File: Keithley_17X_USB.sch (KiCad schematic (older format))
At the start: 39 parts, among them J1 USB_B, J2 SIGNAL INPUT, J3 PROG, U1 TLP281-4, U2 TLP281-4, U3 MIC5504-3.3YM5, U4 MSP430FR2110, U5 FT230XS

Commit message: add right angle mount
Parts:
- H5, H6: footprint (none) -> Terminal_Keystone:Keystone_Screw-Terminal_7761_RightAngle; Description (none) -> TERM SCREW M3 4 PIN PCB RA; Manufacture (none) -> Keystone Electronics; Mfg Part Number (none) -> 7761; Supplier (none) -> Digi-Key; Supplier Part Number (none) -> 36-7761-ND
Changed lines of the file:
@@
 F 0 "H5" H 6900 6100 50  0000 C CNN
 F 1 "M3_RA" H 6900 6025 50  0000 C CNN
-F 2 "" H 6900 5900 50  0001 C CNN
-F 3 "~" H 6900 5900 50  0001 C CNN
+F 2 "Terminal_Keystone:Keystone_Screw-Terminal_7761_RightAngle" H 6900 5900 50  0001 C CNN
+F 3 "http://www.keyelco.com/product-pdf.cfm?p=3928" H 6900 5900 50  0001 C CNN
+F 4 "TERM SCREW M3 4 PIN PCB RA" H 6900 5900 50  0001 C CNN "Description"
+F 5 "Keystone Electronics" H 6900 5900 50  0001 C CNN "Manufacture"
+F 6 "7761" H 6900 5900 50  0001 C CNN "Mfg Part Number"
+F 7 "Digi-Key" H 6900 5900 50  0001 C CNN "Supplier"
+F 8 "36-7761-ND" H 6900 5900 50  0001 C CNN "Supplier Part Number"
 	1    6900 5900
 	1    0    0    -1
@@
 $Comp
 L Mechanical:MountingHole H6
-U 1 1 5C6C11B3
+U 1 1 5C6C2A25
 P 7300 5900
 F 0 "H6" H 7300 6100 50  0000 C CNN
 F 1 "M3_RA" H 7300 6025 50  0000 C CNN
-F 2 "" H 7300 5900 50  0001 C CNN
-F 3 "~" H 7300 5900 50  0001 C CNN
+F 2 "Terminal_Keystone:Keystone_Screw-Terminal_7761_RightAngle" H 7300 5900 50  0001 C CNN
+F 3 "http://www.keyelco.com/product-pdf.cfm?p=3928" H 7300 5900 50  0001 C CNN
+F 4 "TERM SCREW M3 4 PIN PCB RA" H 7300 5900 50  0001 C CNN "Description"
+F 5 "Keystone Electronics" H 7300 5900 50  0001 C CNN "Manufacture"
+F 6 "7761" H 7300 5900 50  0001 C CNN "Mfg Part Number"
+F 7 "Digi-Key" H 7300 5900 50  0001 C CNN "Supplier"
+F 8 "36-7761-ND" H 7300 5900 50  0001 C CNN "Supplier Part Number"
 	1    7300 5900
 	1    0    0    -1

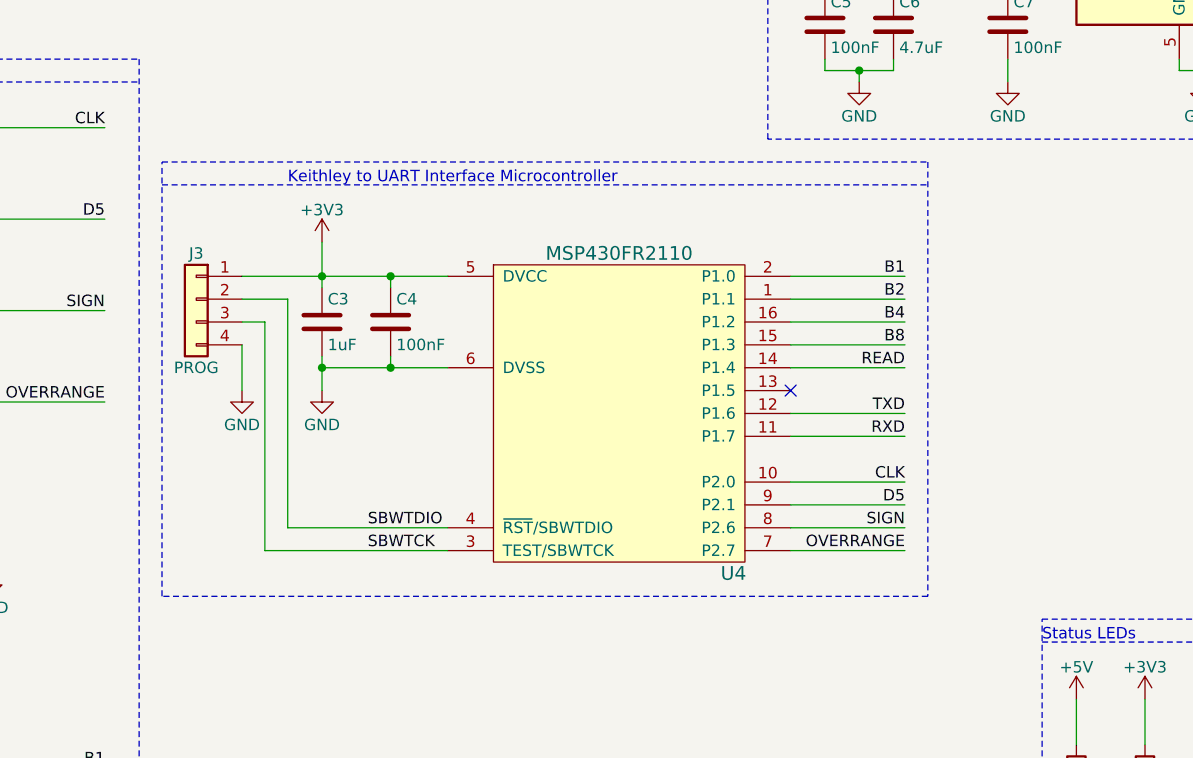
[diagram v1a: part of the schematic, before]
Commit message: added rate selection, trigger on clk or D5. Future implementation
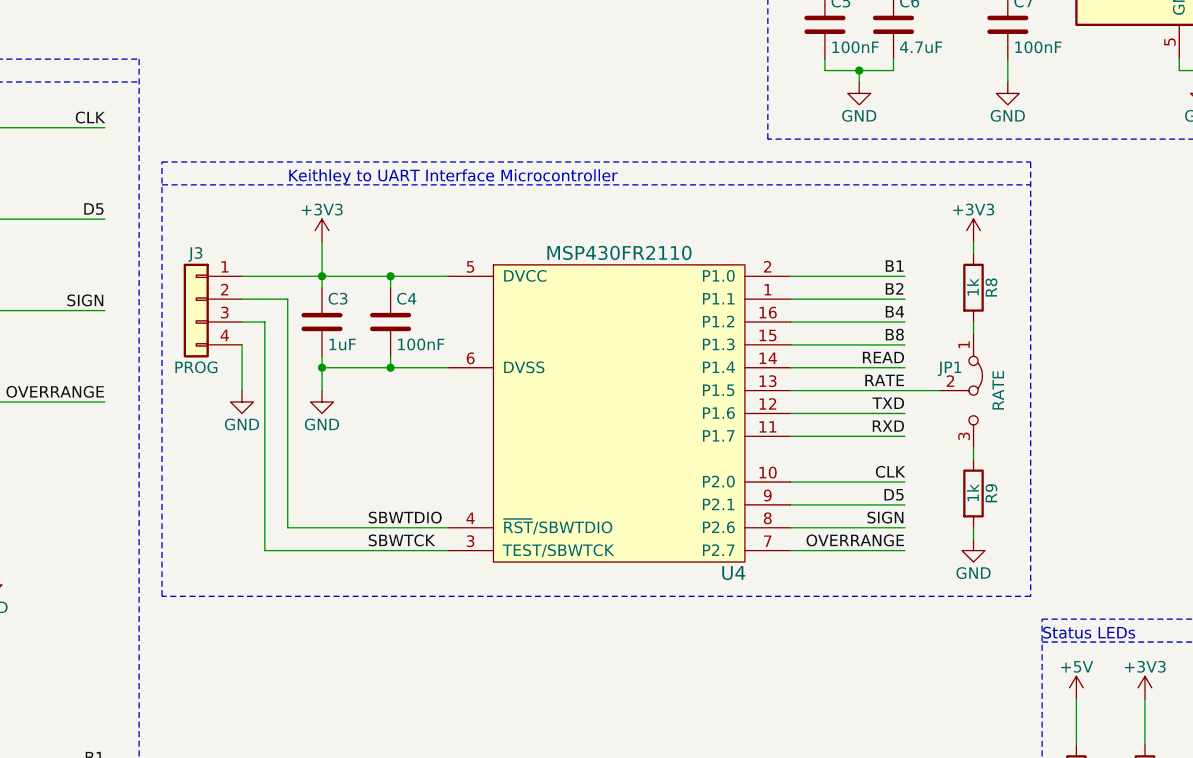
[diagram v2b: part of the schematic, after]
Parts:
- added JP1: RATE, Connector_PinHeader_2.54mm:PinHeader_1x03_P2.54mm_Vertical, symbol Jumper:Jumper_3_Bridged12
- added R8, R9: 1k, Resistor_SMD:R_0603_1608Metric, symbol Device:R
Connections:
- net +3V3: now also R8.1
- net GND: now also R9.2
- net RATE: now reaches U4.13 (P1.5)
- net RATE: now also JP1.2 (C)
- new net: JP1.1 (A), R8.2
- new net: JP1.3 (B), R9.1
- no-connect marks 11 -> 10
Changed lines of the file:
@@
 Text Label 8050 3950 2    50   ~ 0
 READ
-NoConn ~ 7550 4050
 Wire Wire Line
 	5800 3550 6050 3550
@@
 Keithley to UART Interface Microcontroller
 Wire Notes Line
-	4800 3150 8150 3150
-Wire Notes Line
-	8150 4950 4800 4950
+	4800 3150 8600 3150
+Wire Notes Line
+	8600 4950 4800 4950
 Wire Notes Line
 	4800 4950 4800 3050
 Wire Notes Line
-	4800 3050 8150 3050
-Wire Notes Line
-	8150 3050 8150 4950
+	4800 3050 8600 3050
+Wire Notes Line
+	8600 3050 8600 4950
 Text Notes 3000 650  0    50   ~ 0
 3.3V Low Drop Out Regulator
@@
 	1    0    0    -1
 $EndComp
+$Comp
+L Jumper:Jumper_3_Bridged12 JP1
+U 1 1 5C6FA2BD
+P 8350 4050
+F 0 "JP1" V 8250 3950 50  0000 C CNN
+F 1 "RATE" H 8350 4160 50  0000 C CNN
+F 2 "Connector_PinHeader_2.54mm:PinHeader_1x03_P2.54mm_Vertical" H 8350 4050 50  0001 C CNN
+F 3 "~" H 8350 4050 50  0001 C CNN
+	1    8350 4050
+	0    1    1    0
+$EndComp
+Wire Wire Line
+	7550 4050 8200 4050
+$Comp
+L Device:R R8
+U 1 1 5C7417CF
+P 8350 3600
+F 0 "R8" V 8430 3600 50  0000 C CNN
+F 1 "1k" V 8350 3600 50  0000 C CNN
+F 2 "Resistor_SMD:R_0603_1608Metric" V 8280 3600 50  0001 C CNN
+F 3 "http://www.yageo.com/documents/recent/PYu-RC_Group_51_RoHS_L_10.pdf" H 8350 3600 50  0001 C CNN
+F 4 "RES SMD 1K OHM 5% 1/10W 0603" H -1900 -2150 50  0001 C CNN "Description"
+F 5 "Yageo" H -1900 -2150 50  0001 C CNN "Manufacture"
+F 6 "RC0603JR-071KL" H -1900 -2150 50  0001 C CNN "Mfg Part Number"
+F 7 "Digi-Key" H -1900 -2150 50  0001 C CNN "Supplier"
+F 8 "311-1.0KGRCT-ND" H -1900 -2150 50  0001 C CNN "Supplier Part Number"
+	1    8350 3600
+	1    0    0    -1
+$EndComp
+$Comp
+L Device:R R9
+U 1 1 5C7418A1
+P 8350 4500
+F 0 "R9" V 8430 4500 50  0000 C CNN
+F 1 "1k" V 8350 4500 50  0000 C CNN
+F 2 "Resistor_SMD:R_0603_1608Metric" V 8280 4500 50  0001 C CNN
+F 3 "http://www.yageo.com/documents/recent/PYu-RC_Group_51_RoHS_L_10.pdf" H 8350 4500 50  0001 C CNN
+F 4 "RES SMD 1K OHM 5% 1/10W 0603" H -1900 -1250 50  0001 C CNN "Description"
+F 5 "Yageo" H -1900 -1250 50  0001 C CNN "Manufacture"
+F 6 "RC0603JR-071KL" H -1900 -1250 50  0001 C CNN "Mfg Part Number"
+F 7 "Digi-Key" H -1900 -1250 50  0001 C CNN "Supplier"
+F 8 "311-1.0KGRCT-ND" H -1900 -1250 50  0001 C CNN "Supplier Part Number"
+	1    8350 4500
+	1    0    0    -1
+$EndComp
+$Comp
+L power:+3V3 #PWR0103
+U 1 1 5C741A3C
+P 8350 3400
+F 0 "#PWR0103" H 8350 3250 50  0001 C CNN
+F 1 "+3V3" H 8350 3540 50  0000 C CNN
+F 2 "" H 8350 3400 50  0001 C CNN
+F 3 "" H 8350 3400 50  0001 C CNN
+	1    8350 3400
+	1    0    0    -1
+$EndComp
+$Comp
+L power:GND #PWR0104
+U 1 1 5C741A9B
+P 8350 4700
+F 0 "#PWR0104" H 8350 4450 50  0001 C CNN
+F 1 "GND" H 8350 4550 50  0000 C CNN
+F 2 "" H 8350 4700 50  0001 C CNN
+F 3 "" H 8350 4700 50  0001 C CNN
+	1    8350 4700
+	1    0    0    -1
+$EndComp
+Wire Wire Line
+	8350 4700 8350 4650
+Wire Wire Line
+	8350 3800 8350 3750
+Wire Wire Line
+	8350 3450 8350 3400
+Wire Wire Line
+	8350 4350 8350 4300
+Text Label 8050 4050 2    50   ~ 0
+RATE
 $EndSCHEMATC

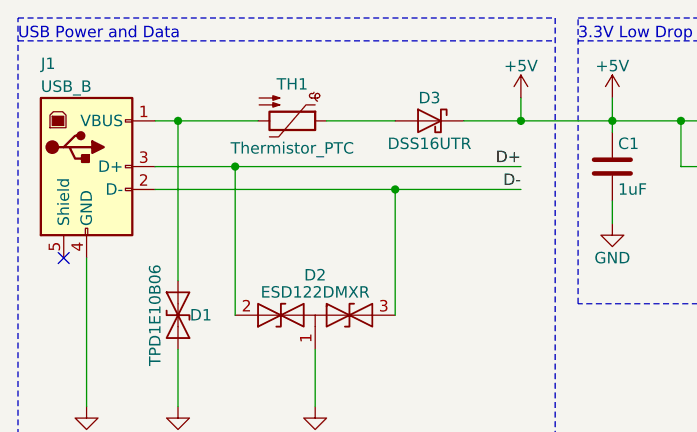
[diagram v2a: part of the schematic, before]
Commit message: change TH1 name to part number
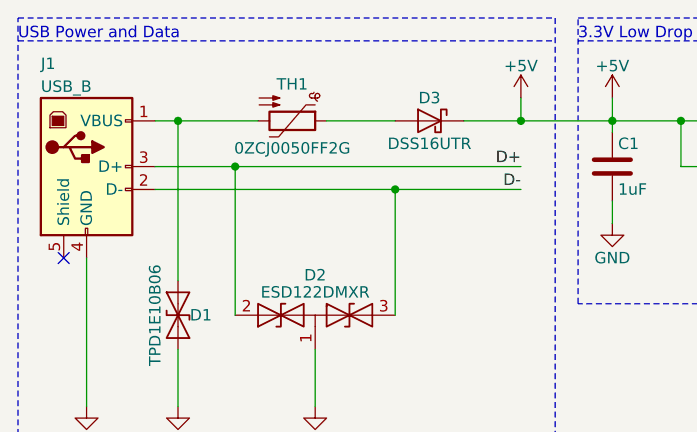
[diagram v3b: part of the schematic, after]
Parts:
- TH1: value Thermistor_PTC -> 0ZCJ0050FF2G
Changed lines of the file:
@@
 P 1750 1000
 F 0 "TH1" V 1590 1000 50  0000 C CNN
-F 1 "Thermistor_PTC" V 1870 1000 50  0000 C CNN
+F 1 "0ZCJ0050FF2G" V 1870 1000 50  0000 C CNN
 F 2 "Fuse:Fuse_1206_3216Metric" H 1800 800 50  0001 L CNN
 F 3 "https://www.belfuse.com/resources/CircuitProtection/datasheets/0ZCJ%20Nov2016.pdf" H 1750 1000 50  0001 C CNN

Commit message: rearaned B1 B2 B4 and B8 connection to opto for better layout
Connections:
- net B1: now also U2.10; no longer U2.16
- net B1_IN: now also U2.7; no longer U2.1
- net B2: now also U2.12; no longer U2.14
- net B2_IN: now also U2.5; no longer U2.3
- net B4: now also U2.14; no longer U2.12
- net B4_IN: now also U2.3; no longer U2.5
- net B8: now also U2.16; no longer U2.10
- net B8_IN: now also U2.1; no longer U2.7
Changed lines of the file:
@@
 Text Label 2250 4100 0    50   ~ 0
 OVERRANGE_IN
+Text Label 2250 6900 0    50   ~ 0
+B1_IN
+Text Label 2250 6500 0    50   ~ 0
+B2_IN
+Text Label 2250 6100 0    50   ~ 0
+B4_IN
 Text Label 2250 5700 0    50   ~ 0
-B1_IN
-Text Label 2250 6100 0    50   ~ 0
-B2_IN
-Text Label 2250 6500 0    50   ~ 0
-B4_IN
-Text Label 2250 6900 0    50   ~ 0
 B8_IN
 Wire Wire Line
@@
 Text Label 4550 4100 2    50   ~ 0
 OVERRANGE
+Text Label 4550 6900 2    50   ~ 0
+B1
+Text Label 4550 6500 2    50   ~ 0
+B2
+Text Label 4550 6100 2    50   ~ 0
+B4
 Text Label 4550 5700 2    50   ~ 0
-B1
-Text Label 4550 6100 2    50   ~ 0
-B2
-Text Label 4550 6500 2    50   ~ 0
-B4
-Text Label 4550 6900 2    50   ~ 0
 B8
 Wire Wire Line
@@
 	3250 3300 1100 3300
 Wire Wire Line
-	1000 5700 1000 5200
-Wire Wire Line
-	3250 5700 1000 5700
-Wire Wire Line
-	900  6100 900  5100
-Wire Wire Line
-	3250 6100 900  6100
+	1000 6900 1000 5200
+Wire Wire Line
+	3250 6900 1000 6900
+Wire Wire Line
+	900  6500 900  5100
+Wire Wire Line
+	3250 6500 900  6500
 Wire Wire Line
 	1350 5100 900  5100
 Wire Wire Line
-	800  6500 800  5000
-Wire Wire Line
-	3250 6500 800  6500
+	800  6100 800  5000
+Wire Wire Line
+	3250 6100 800  6100
 Wire Wire Line
 	1350 5000 800  5000
 Wire Wire Line
-	700  6900 700  4900
-Wire Wire Line
-	3250 6900 700  6900
+	700  5700 700  4900
+Wire Wire Line
+	3250 5700 700  5700
 Wire Wire Line
 	1350 4900 700  4900

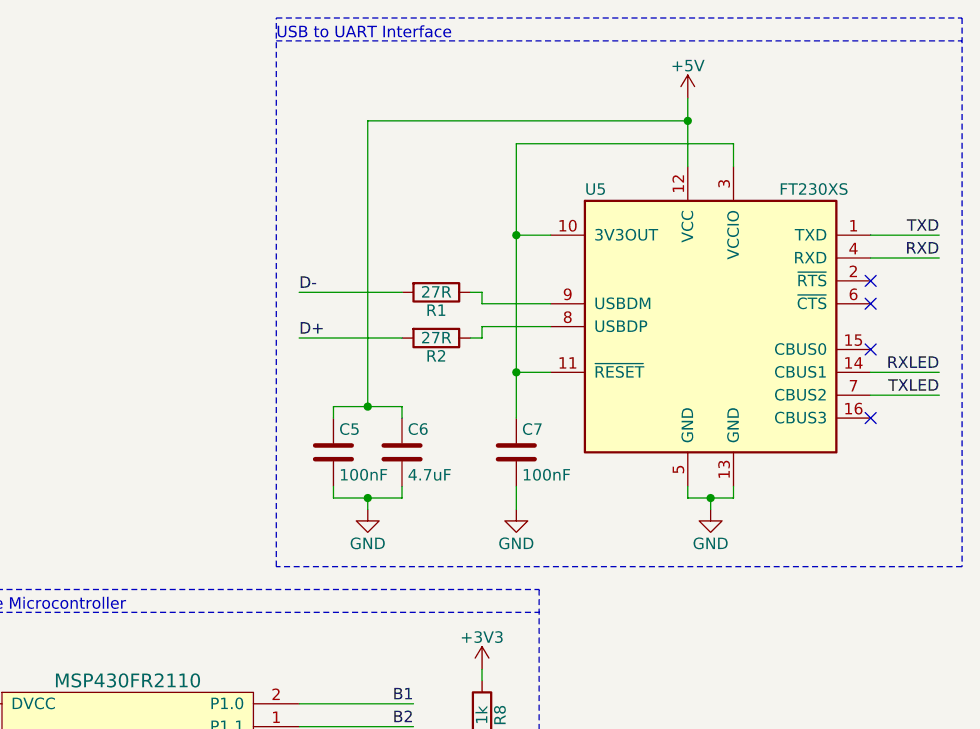
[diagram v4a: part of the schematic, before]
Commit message: lable right side of usb data lines for differential pair routing
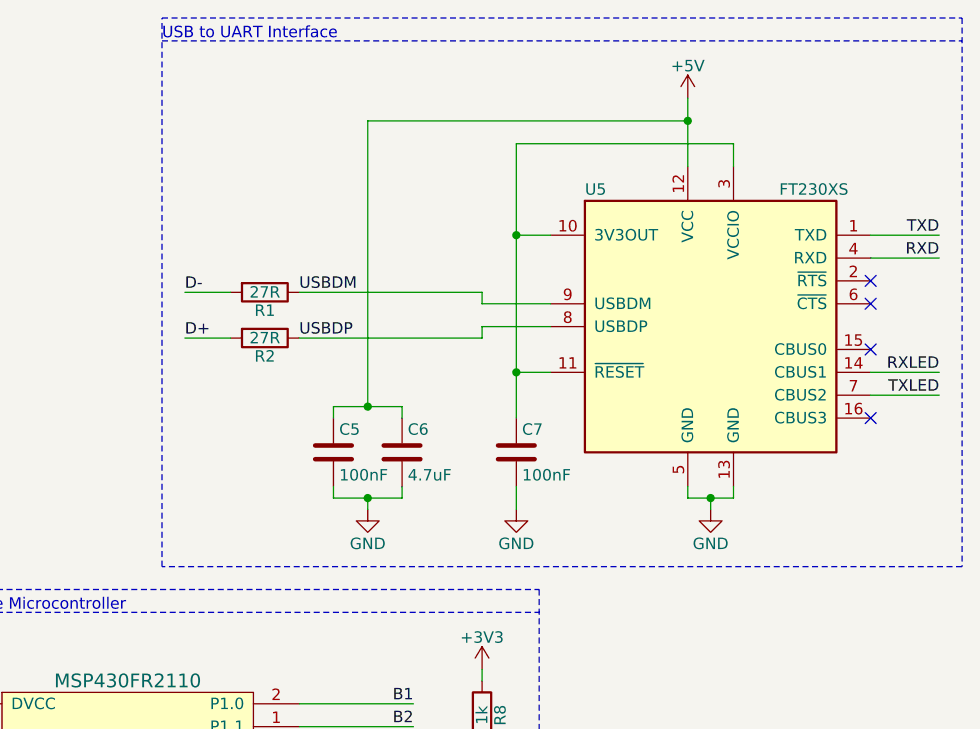
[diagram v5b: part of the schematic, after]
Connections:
- net USBDP: now reaches R2.1, U5.8 (USBDP)
- net USBDM: now reaches R1.1, U5.9 (USBDM)
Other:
- moved on the sheet: R1, R2
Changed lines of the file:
@@
 L Device:R R1
 U 1 1 5C60A39E
-P 8150 1750
-F 0 "R1" V 8230 1750 50  0000 C CNN
-F 1 "27R" V 8150 1750 50  0000 C CNN
-F 2 "Resistor_SMD:R_0603_1608Metric" V 8080 1750 50  0001 C CNN
-F 3 "https://www.seielect.com/Catalog/SEI-RMCF_RMCP.pdf" H 8150 1750 50  0001 C CNN
-F 4 "RES 27 OHM 5% 1/10W 0603" H 0   0   50  0001 C CNN "Description"
-F 5 "Stackpole Electronics Inc" H 0   0   50  0001 C CNN "Manufacture"
-F 6 "RMCF0603JT27R0" H 0   0   50  0001 C CNN "Mfg Part Number"
-F 7 "Digi-Key" H 0   0   50  0001 C CNN "Supplier"
-F 8 "RMCF0603JT27R0CT-ND" H 0   0   50  0001 C CNN "Supplier Part Number"
-	1    8150 1750
+P 7400 1750
+F 0 "R1" V 7480 1750 50  0000 C CNN
+F 1 "27R" V 7400 1750 50  0000 C CNN
+F 2 "Resistor_SMD:R_0603_1608Metric" V 7330 1750 50  0001 C CNN
+F 3 "https://www.seielect.com/Catalog/SEI-RMCF_RMCP.pdf" H 7400 1750 50  0001 C CNN
+F 4 "RES 27 OHM 5% 1/10W 0603" H -750 0   50  0001 C CNN "Description"
+F 5 "Stackpole Electronics Inc" H -750 0   50  0001 C CNN "Manufacture"
+F 6 "RMCF0603JT27R0" H -750 0   50  0001 C CNN "Mfg Part Number"
+F 7 "Digi-Key" H -750 0   50  0001 C CNN "Supplier"
+F 8 "RMCF0603JT27R0CT-ND" H -750 0   50  0001 C CNN "Supplier Part Number"
+	1    7400 1750
 	0    1    1    0
 $EndComp
@@
 L Device:R R2
 U 1 1 5C60A3D9
-P 8150 1950
-F 0 "R2" V 8230 1950 50  0000 C CNN
-F 1 "27R" V 8150 1950 50  0000 C CNN
-F 2 "Resistor_SMD:R_0603_1608Metric" V 8080 1950 50  0001 C CNN
-F 3 "https://www.seielect.com/Catalog/SEI-RMCF_RMCP.pdf" H 8150 1950 50  0001 C CNN
-F 4 "RES 27 OHM 5% 1/10W 0603" H 0   0   50  0001 C CNN "Description"
-F 5 "Stackpole Electronics Inc" H 0   0   50  0001 C CNN "Manufacture"
-F 6 "RMCF0603JT27R0" H 0   0   50  0001 C CNN "Mfg Part Number"
-F 7 "Digi-Key" H 0   0   50  0001 C CNN "Supplier"
-F 8 "RMCF0603JT27R0CT-ND" H 0   0   50  0001 C CNN "Supplier Part Number"
-	1    8150 1950
+P 7400 1950
+F 0 "R2" V 7480 1950 50  0000 C CNN
+F 1 "27R" V 7400 1950 50  0000 C CNN
+F 2 "Resistor_SMD:R_0603_1608Metric" V 7330 1950 50  0001 C CNN
+F 3 "https://www.seielect.com/Catalog/SEI-RMCF_RMCP.pdf" H 7400 1950 50  0001 C CNN
+F 4 "RES 27 OHM 5% 1/10W 0603" H -750 0   50  0001 C CNN "Description"
+F 5 "Stackpole Electronics Inc" H -750 0   50  0001 C CNN "Manufacture"
+F 6 "RMCF0603JT27R0" H -750 0   50  0001 C CNN "Mfg Part Number"
+F 7 "Digi-Key" H -750 0   50  0001 C CNN "Supplier"
+F 8 "RMCF0603JT27R0CT-ND" H -750 0   50  0001 C CNN "Supplier Part Number"
+	1    7400 1950
 	0    1    1    0
 $EndComp
@@
 	8350 1800 8350 1750
 Wire Wire Line
-	8350 1750 8300 1750
+	8350 1750 7550 1750
 Wire Wire Line
 	8650 1900 8350 1900
@@
 	8350 1900 8350 1950
 Wire Wire Line
-	8350 1950 8300 1950
+	8350 1950 7550 1950
 $Comp
 L power:GND #PWR01
@@
 	7850 2250 8000 2250
 Wire Wire Line
-	8000 1750 7550 1750
-Wire Wire Line
-	8000 1950 7550 1950
-Text Notes 7450 650  0    50   ~ 0
+	7250 1750 7050 1750
+Wire Wire Line
+	7250 1950 7050 1950
+Text Notes 6950 650  0    50   ~ 0
 USB to UART Interface
 Wire Notes Line
-	7450 650  10450 650
-Wire Notes Line
-	10450 2950 7450 2950
-Wire Notes Line
-	7450 2950 7450 550
-Wire Notes Line
-	7450 550  10450 550
+	6950 650  10450 650
+Wire Notes Line
+	10450 2950 6950 2950
+Wire Notes Line
+	6950 2950 6950 550
+Wire Notes Line
+	6950 550  10450 550
 Wire Notes Line
 	10450 550  10450 2950
-Text Label 7550 1950 0    50   ~ 0
+Text Label 7050 1950 0    50   ~ 0
 D+
-Text Label 7550 1750 0    50   ~ 0
+Text Label 7050 1750 0    50   ~ 0
 D-
 Text Notes 5350 3150 0    50   ~ 0
@@
 Text Label 8050 4050 2    50   ~ 0
 RATE
+Text Label 7550 1750 0    50   ~ 0
+USBDM
+Text Label 7550 1950 0    50   ~ 0
+USBDP
 $EndSCHEMATC
